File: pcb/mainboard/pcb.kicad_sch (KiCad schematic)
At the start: 0 parts

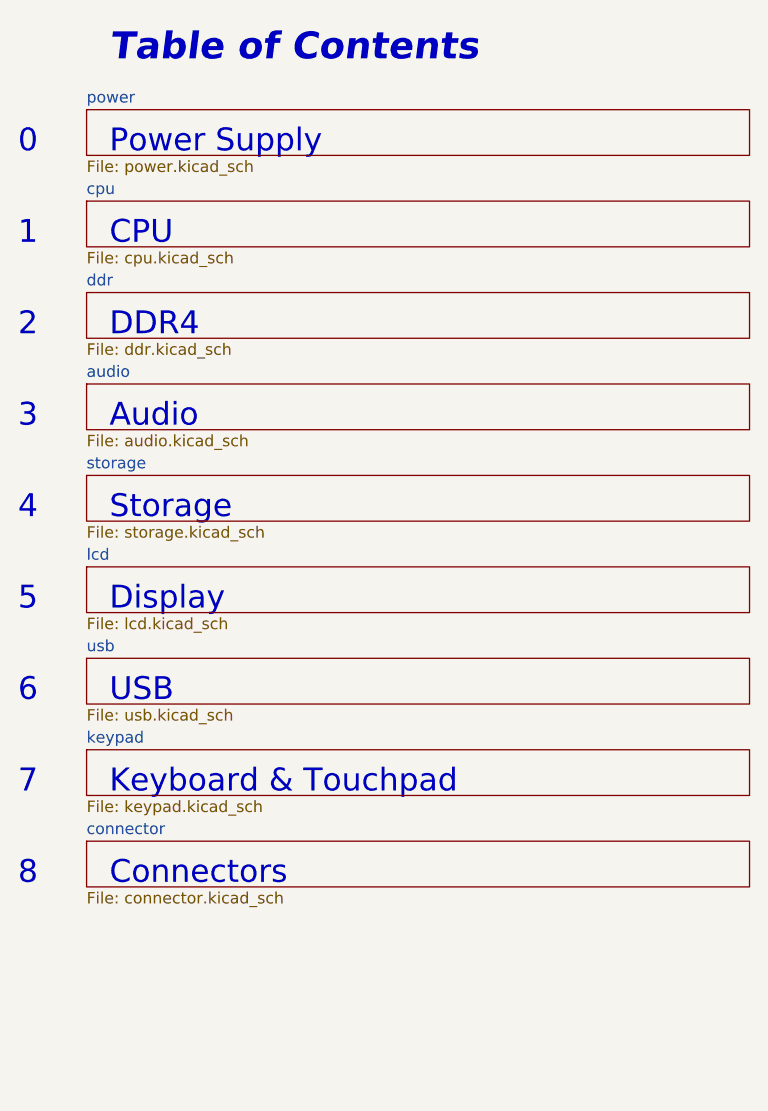
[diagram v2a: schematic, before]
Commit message: - pcb: switch to imx7 for the prototype
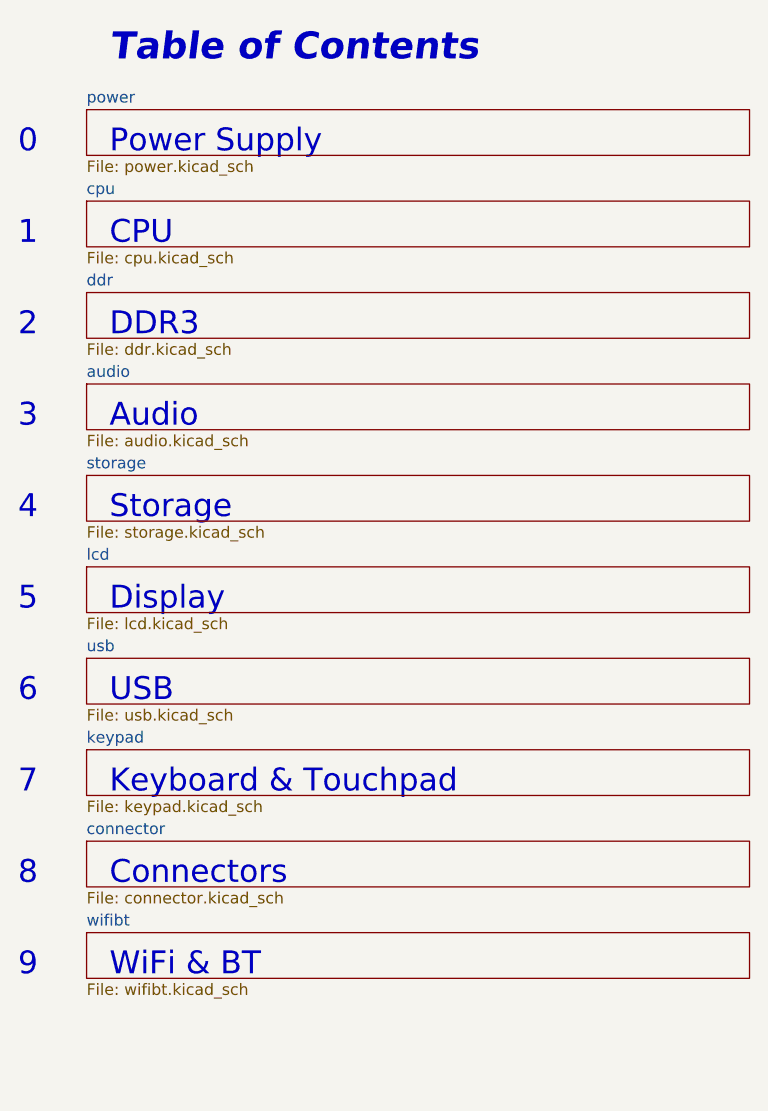
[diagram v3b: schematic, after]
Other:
- added sheet wifibt (wifibt.kicad_sch)
- note added: "9"
- note added: "DDR3"
- note added: "WiFi & BT"
- note removed: "DDR4"

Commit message: - pcb: working on r0p1 sch
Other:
- removed sheet connector
- added sheet ec (ec.kicad_sch)
- note added: "EC"
- note added: "Keyboard"
- note removed: "Connectors"
- note removed: "Keyboard & Touchpad"

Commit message: - pcb: start r0p1 layout
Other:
- company: Copyright EI-2030 2021. -> Copyright EI-2030 2021. / Engineer: Wenting Zhang
- title: Archer -> Archer Mainboard

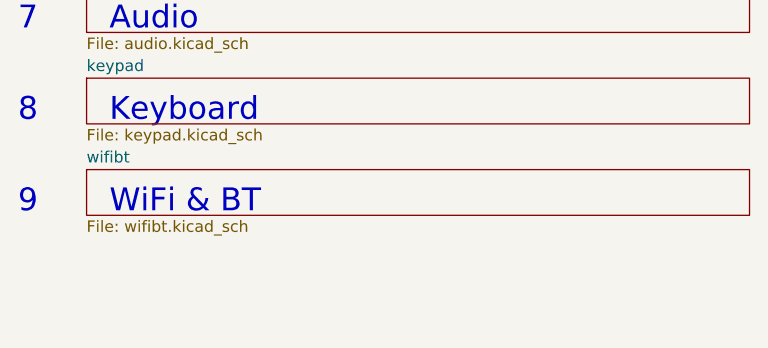
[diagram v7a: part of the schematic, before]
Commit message: - pcb: components placed
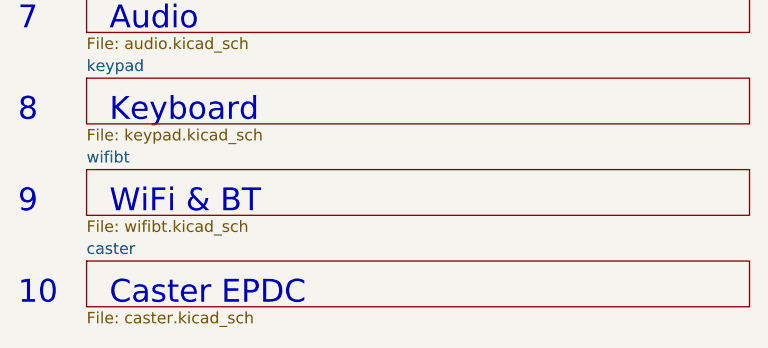
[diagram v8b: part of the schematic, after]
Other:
- added sheet caster (caster.kicad_sch)
- note added: "10"
- note added: "Caster EPDC"
